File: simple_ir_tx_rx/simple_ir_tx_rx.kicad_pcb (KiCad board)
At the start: 2 copper layers, 19.2 x 14.5 mm, 14 parts, among them J1 CONN_01X05, Q1 Q_NMOS_GSD, Q2 Q_PMOS_GSD, U1 TSOP45xx

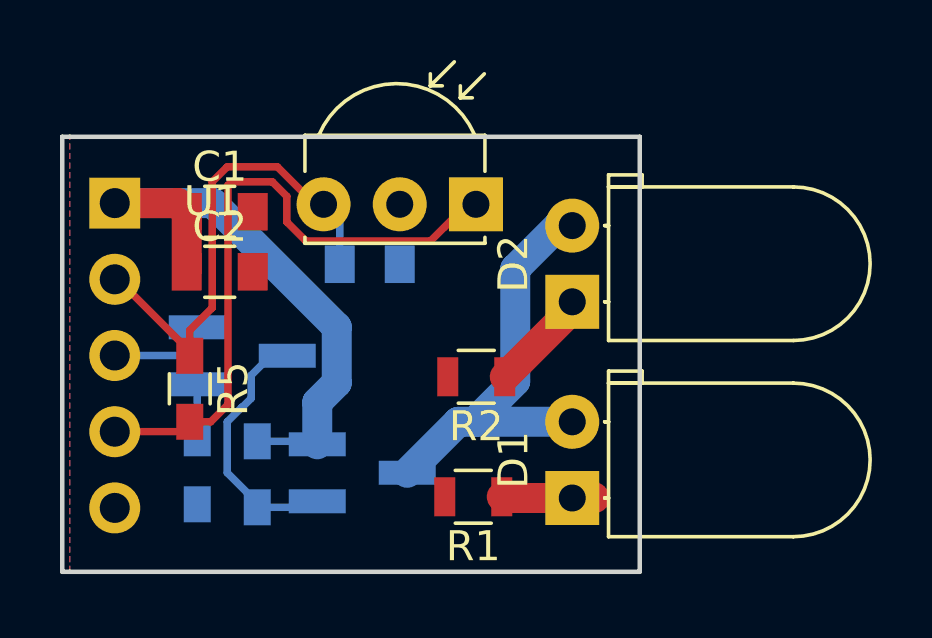
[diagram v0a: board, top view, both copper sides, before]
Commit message: Changed gerber generation settings, added PCB text
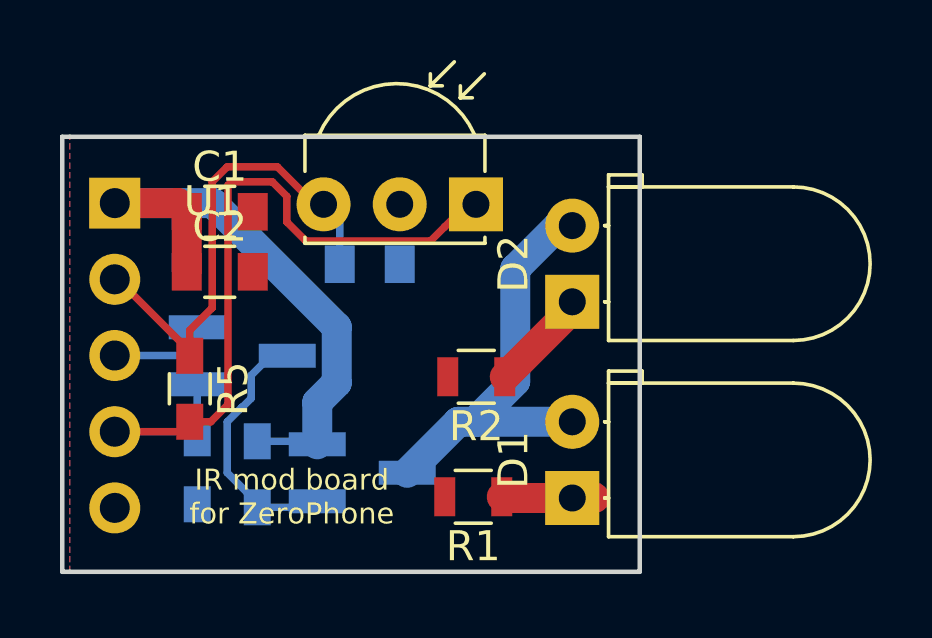
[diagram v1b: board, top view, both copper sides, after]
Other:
- board text added: "IR mod board for ZeroPhone"
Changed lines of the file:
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@@
   (general
     (links 25)
-    (no_connects 5)
-    (area 129.174999 102.424999 148.575001 117.075001)
+    (no_connects 0)
+    (area 120.224999 99.739999 158.255 118.215)
     (thickness 1.6)
-    (drawings 6)
+    (drawings 7)
     (tracks 63)
     (zones 0)
@@
     (pad_drill 0)
     (pad_to_mask_clearance 0.2)
-    (aux_axis_origin 0 0)
-    (visible_elements FFFFFF7F)
+    (aux_axis_origin 128.6 102.1)
+    (visible_elements 7FFFFFFF)
     (pcbplotparams
-      (layerselection 0x00030_80000001)
-      (usegerberextensions false)
+      (layerselection 0x010f0_80000001)
+      (usegerberextensions true)
+      (usegerberattributes true)
       (excludeedgelayer true)
       (linewidth 0.100000)
@@
       (viasonmask false)
       (mode 1)
-      (useauxorigin false)
+      (useauxorigin true)
       (hpglpennumber 1)
       (hpglpenspeed 20)
@@
       (psnegative false)
       (psa4output false)
-      (plotreference true)
-      (plotvalue true)
+      (plotreference false)
+      (plotvalue false)
       (plotinvisibletext false)
       (padsonsilk false)
@@
       (outputformat 1)
       (mirror false)
-      (drillshape 1)
+      (drillshape 0)
       (scaleselection 1)
-      (outputdirectory ""))
+      (outputdirectory gerbers/))
   )
   (net 0 "")
@@
     )
   )
+  (gr_text "IR mod board\nfor ZeroPhone" (at 136.9 114.5) (layer F.SilkS)
+    (effects (font (size 0.7 0.7) (thickness 0.175)))
+  )
   (gr_line (start 129.5 117) (end 129.25 117) (layer Edge.Cuts) (width 0.15))

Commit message: Changed connector (to clean silkscreen)
Also, fixed potential acid trap place
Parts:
- J1: footprint Pin_Headers:Pin_Header_Angled_1x05_Pitch2.54mm -> Pin_Headers:Pin_Header_Straight_1x05_Pitch2.54mm
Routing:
- net Net-(D1-Pad2): track 14.4 -> 19.2 mm

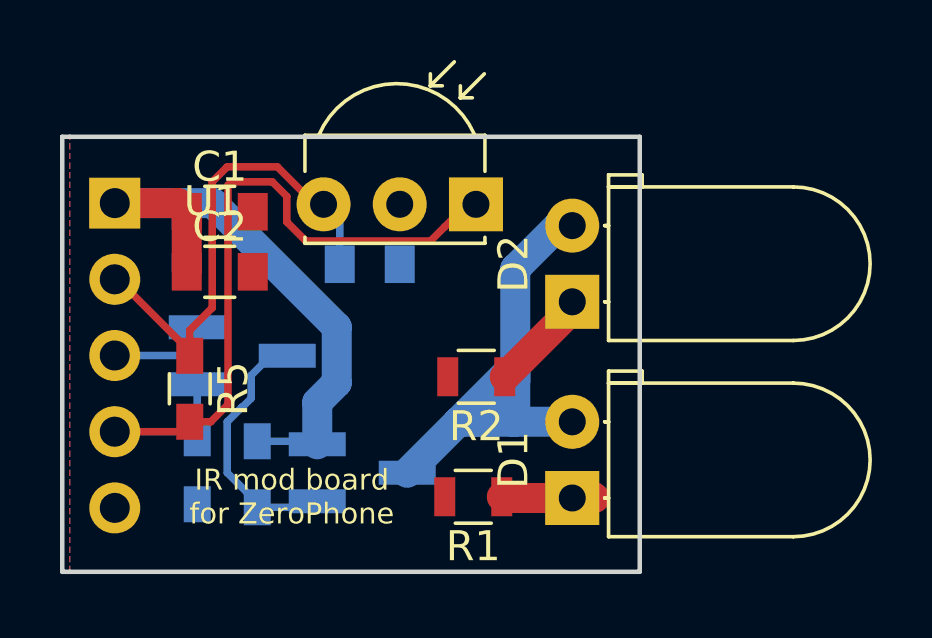
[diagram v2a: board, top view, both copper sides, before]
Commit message: Added version information, updated pinout
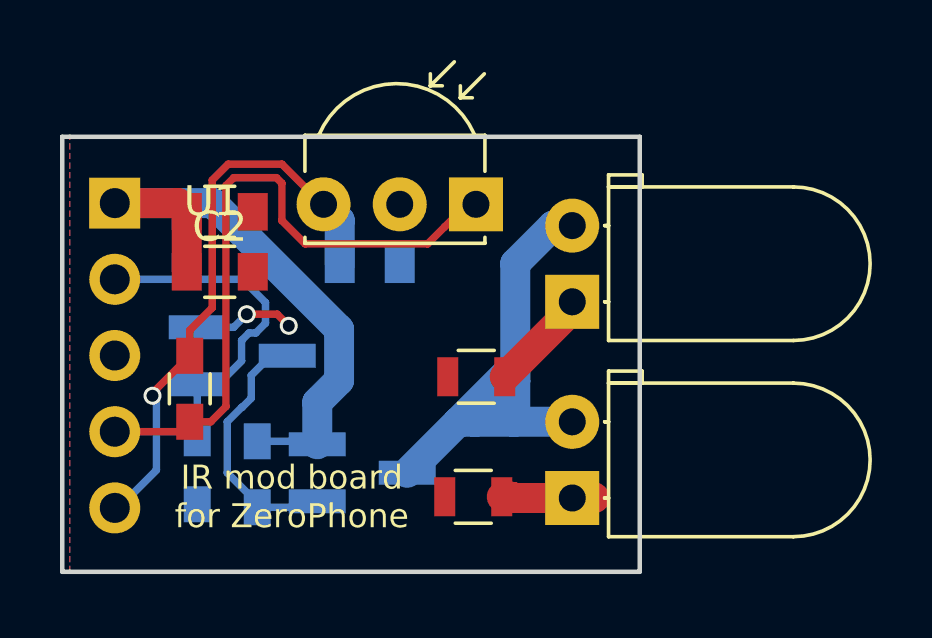
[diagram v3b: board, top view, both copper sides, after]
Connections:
- J1 pad 2: +3V3 -> IR_TX
- J1 pad 3: IR_TX -> GND
- J1 pad 5: GND -> +3V3
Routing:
- net IR_TX: track 5.33 -> 11.5 mm
- net GND: track 0.00 -> 3.39 mm, vias 0 -> 2
- net +3V3: track 16.1 -> 19.5 mm, vias 0 -> 1
- net IR_RX: track 21.7 -> 22.4 mm
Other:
- board text added: "v1.0"
